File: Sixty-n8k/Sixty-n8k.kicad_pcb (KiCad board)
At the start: 4 copper layers, 149.9 x 99.7 mm, 67 parts, among them J1 USB4085-GF-A_REVB, J2 SD_CARD_PORT, J3 Conn_02x32_Odd_Even, J4 Conn_01x02, SW1 RESET, SW2 DEBUG, U1 74LS05, U10 74HC164, U11 74LS393, U12 22V10C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

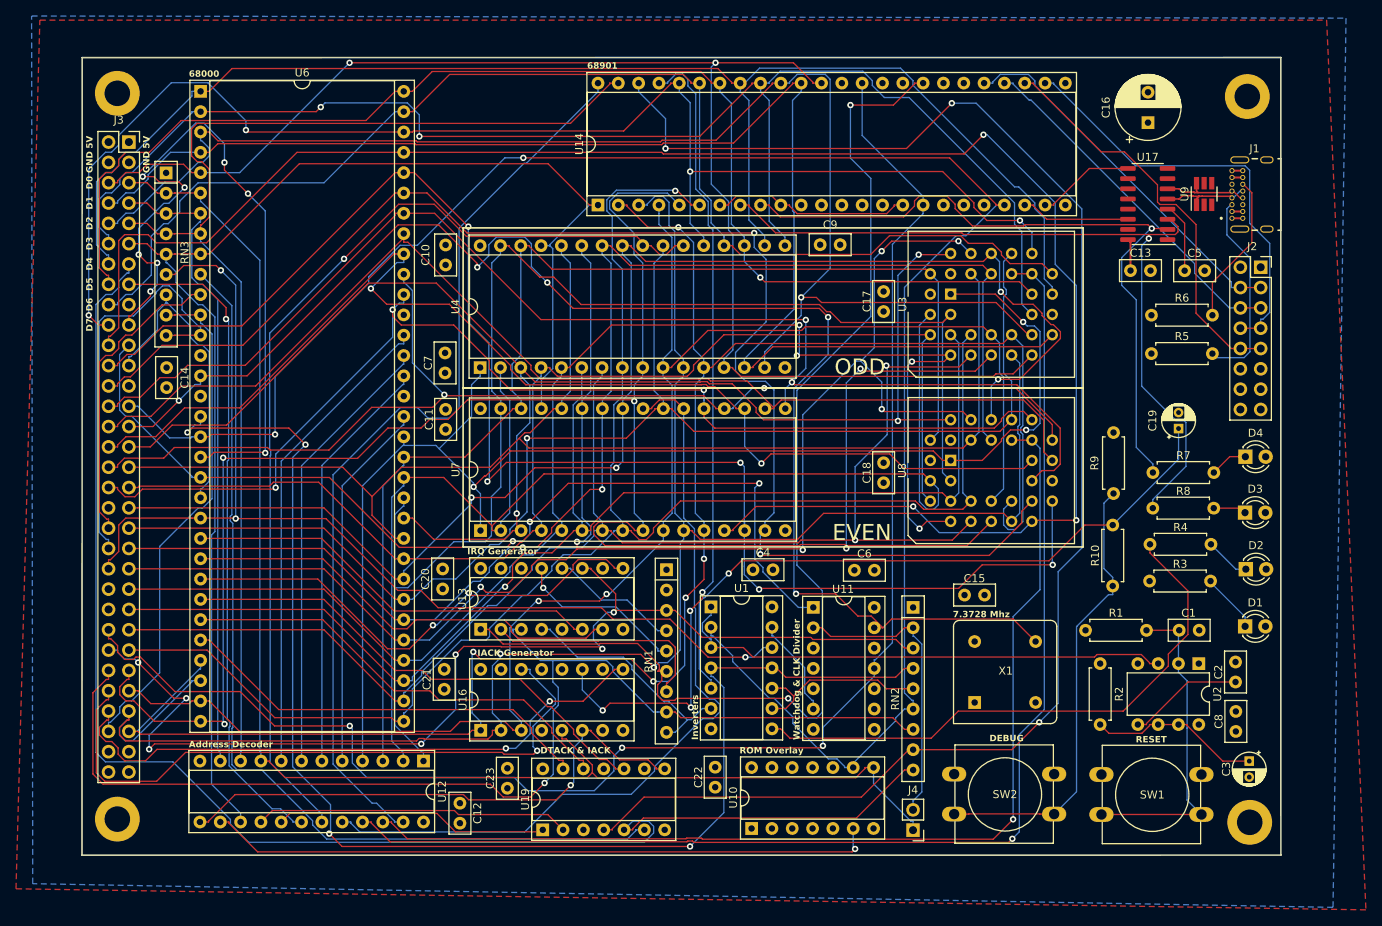
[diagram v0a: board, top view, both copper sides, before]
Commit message: Adds GAL logic
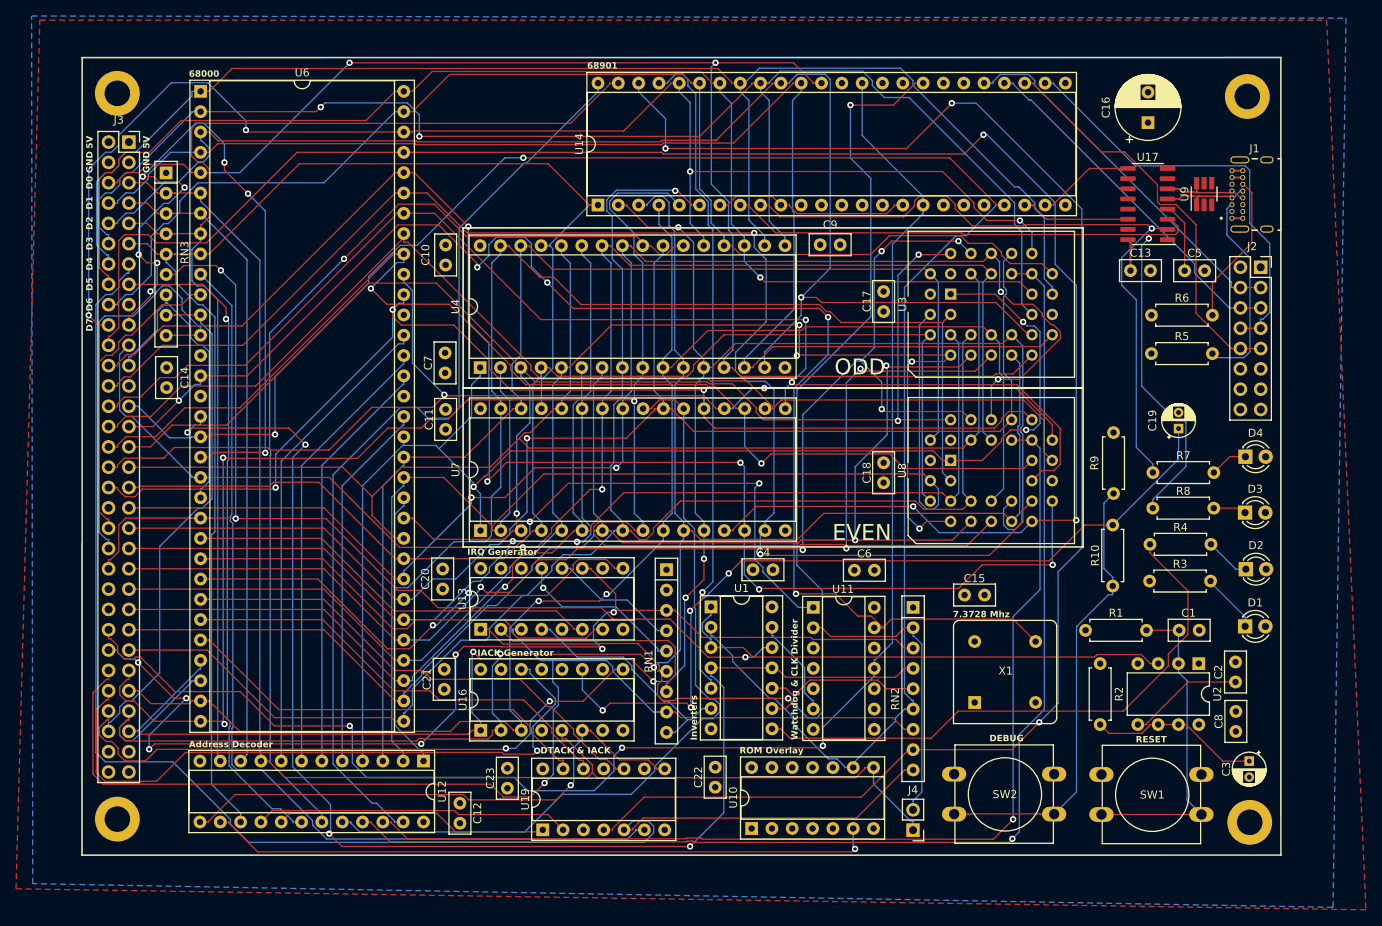
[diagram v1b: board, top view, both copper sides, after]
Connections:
- net ~{DTACK_RAM} renamed ~{CS_RAM}
- net ~{DTACK_ROM} renamed ~{CS_ROM}
- U12 pad 10: ~{LDS} -> ~{UDS}
- U12 pad 11: ~{UDS} -> ~{LDS}
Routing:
- net +5V: track 6.71 -> 12.9 mm
- net GND: track 2.70 -> 4.82 mm
- net ~{LDS}: track 148.3 -> 148.9 mm

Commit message: Removed pullup on RWb
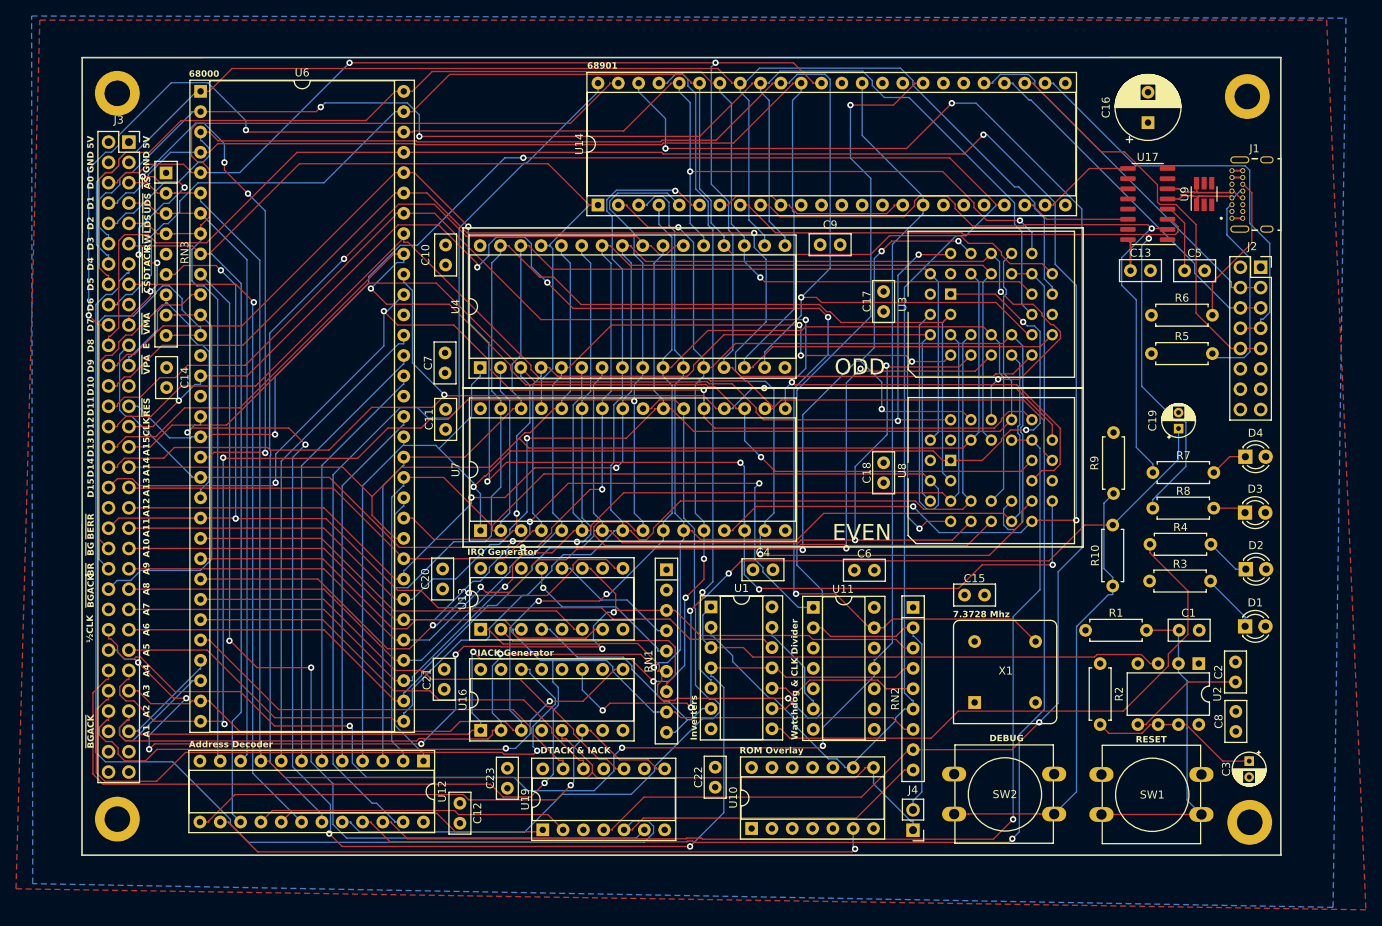
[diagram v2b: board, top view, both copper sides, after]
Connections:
- J3 pad 40: ~{BG} -> ~{BERR}
- J3 pad 42: ~{BR} -> ~{BG}
- J3 pad 44: ~{BERR} -> ~{BR}
- J3 pad 46: unconnected-(J3-Pin_46-Pad46) -> ~{BGACK}
- J3 pad 60: ~{BGACK} -> unconnected-(J3-Pin_60-Pad60)
- RN3 pad 5: R~{W} -> unconnected-(RN3-R4-Pad5)
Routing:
- net ~{BGACK}: track 63.3 -> 49.9 mm
- net ~{BERR}: track 135.2 -> 129.5 mm, vias 3 -> 2
- net /A8: track 172.8 -> 167.6 mm
- net ~{BG}: track 38.0 -> 40.4 mm
- net ~{BR}: track 52.0 -> 54.3 mm
- net /D13: track 150.1 -> 149.0 mm
- net CLK_{CPU}: track 180.0 -> 178.9 mm
- net ~{CS_XPN}: track 83.0 -> 84.1 mm
- net R~{W}: track 172.0 -> 171.2 mm
- net ~{DTACK}: track 119.4 -> 119.8 mm, vias 0 -> 2
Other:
- board text added: "A1"
- board text added: "A10"
- board text added: "A11"
- board text added: "A12"
- board text added: "A13"
- board text added: "A14"
- board text added: "A15"
- board text added: "A2"
- board text added: "A3"
- board text added: "A4"
- board text added: "A5"
- board text added: "A6"
- board text added: "A7"
- board text added: "A8"
- board text added: "A9"
- board text added: "CLK"
- board text added: "D10"
- board text added: "D11"
- board text added: "D12"
- board text added: "D13"
- board text added: "D14"
- board text added: "D15"
- board text added: "D8"
- board text added: "D9"
- board text added: "E"
- board text added: "R~{W}"
- board text added: "~{AS}"
- board text added: "~{BERR}"
- board text added: "~{BGACK}"
- board text added: "~{BG}"
- board text added: "~{BR}"
- board text added: "~{CS}"
- board text added: "~{DTACK}"
- board text added: "~{LDS}"
- board text added: "~{RES}"
- board text added: "~{UDS}"
- board text added: "~{VMA}"
- board text added: "~{VPA}"
- board text added: "½CLK"

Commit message: Sent to pcb board house
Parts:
- added G1: LOGO, graphics:Shaka, F.Cu at (116.1, 56.4)
- added G2: LOGO, graphics:MadeInAMS, F.Cu at (124.8, 56.2)
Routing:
- net /D13: track 149.0 -> 140.6 mm
- net ~{IRQ_LOW}: track 140.4 -> 135.2 mm, vias 7 -> 4
- net ~{DTACK}: track 119.8 -> 123.2 mm, vias 2 -> 0
- net CLK_{HALF}: track 196.3 -> 193.9 mm
- net RxD: track 88.9 -> 86.9 mm
- net TxD: track 98.0 -> 96.0 mm, vias 1 -> 0
- net /D15: track 143.3 -> 141.5 mm, vias 3 -> 2
- net /A4: track 260.0 -> 258.5 mm
- net ~{DTACK_XPN}: track 183.1 -> 184.5 mm
- net ~{RES}: track 240.8 -> 239.8 mm
- net /A2: track 231.8 -> 230.9 mm
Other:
- board text added: "JLCJLCJLCJLC"
- board text added: "Sixty n8K"
- board text added: "Watchdog?"
- board text added: "by Nate Rivard v1.0 Feb 7, 2024 https://github.com/nrivard/Sixty-n8k"
- board text added: "~{IACK}"
- board text added: "~{IRQ}"
